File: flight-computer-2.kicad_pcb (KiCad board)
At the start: 4 copper layers, 51 x 51 mm, 0 parts

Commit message: Rough PCB layout
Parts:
- added AE1: 47948-0001, flight-computer-2:47948-0001, F.Cu at (97.5, 58.2)
- added C1: 4.7uF, flight-computer-2:C_0603_1608Metric, F.Cu at (176.9, 78.6)
- added C10: 22pF, flight-computer-2:C_0603_1608Metric, F.Cu at (183.7, 68.1)
- added C11: 22pF, flight-computer-2:C_0603_1608Metric, F.Cu at (187.1, 65.5)
- added C12: 0.1uF, flight-computer-2:C_0603_1608Metric, F.Cu at (165.1, 87.9)
- added C13: 10uF, flight-computer-2:C_0603_1608Metric, F.Cu at (188.6, 62.3)
- added C14: 1uF, flight-computer-2:C_0603_1608Metric, F.Cu at (192.6, 62.3)
- added C15: 0.1uF, flight-computer-2:C_0603_1608Metric, F.Cu at (163.8, 91.4)
- added C16: 0.1uF, flight-computer-2:C_0603_1608Metric, F.Cu at (183.7, 70.6)
- added C17: 10uF, flight-computer-2:C_0603_1608Metric, F.Cu at (174.1, 82.6)
- added C18: 0.1uF, flight-computer-2:C_0603_1608Metric, F.Cu at (186.1, 83.2)
- added C19: 0.1uF, flight-computer-2:C_0603_1608Metric, F.Cu at (179.9, 90.1)
- added C2: 220uF, flight-computer-2:C_1206_3216Metric, F.Cu at (82.5, 56.0)
- added C20: DNP, flight-computer-2:C_0402_1005Metric, F.Cu at (169.5, 85.5)
- added C21: 0.1uF, flight-computer-2:C_0603_1608Metric, F.Cu at (192.9, 74.8)
- added C22: 0.1uF, flight-computer-2:C_0603_1608Metric, F.Cu at (175.9, 92.6)
- added C23: DNP, flight-computer-2:C_0402_1005Metric, F.Cu at (163.3, 93.7)
- added C3: 220uF, flight-computer-2:C_1206_3216Metric, F.Cu at (166.6, 77.1)
- added C4: 220uF, flight-computer-2:C_1206_3216Metric, F.Cu at (113.0, 99.0)
- added C5: 220uF, flight-computer-2:C_1206_3216Metric, F.Cu at (160.4, 84.2)
- added C6: 4.7uF, flight-computer-2:C_0603_1608Metric, F.Cu at (181.1, 86.1)
- added C7: 0.1uF, flight-computer-2:C_0603_1608Metric, F.Cu at (186.1, 80.7)
- added C8: 0.1uF, flight-computer-2:C_0603_1608Metric, F.Cu at (176.9, 76.1)
- added C9: 0.1uF, flight-computer-2:C_0603_1608Metric, F.Cu at (171.4, 80.1)
- added D1: SM5817PL-TP, flight-computer-2:D_SOD-123F, F.Cu at (160.3, 88.5)
- added D2: LTST-C191KGKT, flight-computer-2:LED_0603_1608Metric, F.Cu at (150.8, 93.7)
- added D3: SM5817PL-TP, flight-computer-2:D_SOD-123F, F.Cu at (172.1, 77.1)
- added D4: USBLC6-2SC6, Package_TO_SOT_SMD:SOT-23-6, F.Cu at (99.0, 89.5)
- added D5: LTST-C191KRKT, flight-computer-2:LED_0603_1608Metric, F.Cu at (183.0, 65.6)
- added D6: LTST-C191TBKT, flight-computer-2:LED_0603_1608Metric, F.Cu at (154.9, 93.7)
- added D7: CLMVC-FKA-CL1D1L71BB7C3C3, flight-computer-2:LED_Cree-PLCC4_2x2mm_CW, F.Cu at (178.8, 72.9)
- added H1: MountingHole, MountingHole:MountingHole_2.2mm_M2, F.Cu at (80.0, 60.0)
- added H2: MountingHole, MountingHole:MountingHole_2.2mm_M2, F.Cu at (115.0, 60.0)
- added H3: MountingHole, MountingHole:MountingHole_2.2mm_M2, F.Cu at (115.0, 95.0)
- added H4: MountingHole, MountingHole:MountingHole_2.2mm_M2, F.Cu at (80.0, 95.0)
- added J1: USB4105-GF-A, flight-computer-2:GCT_USB4105-GF-A, F.Cu at (97.5, 97.8)
- added J2: THR, flight-computer-2:PinHeader_1x03_P2.54mm_Vertical, F.Cu at (88.5, 96.0)
- added J3: SER1, flight-computer-2:PinHeader_1x03_P2.54mm_Vertical, F.Cu at (76.0, 56.0)
- added J4: SER2, flight-computer-2:PinHeader_1x03_P2.54mm_Vertical, F.Cu at (119.0, 56.0)
- added J5: SER3, flight-computer-2:PinHeader_1x03_P2.54mm_Vertical, F.Cu at (119.0, 99.0)
- added J6: SER4, flight-computer-2:PinHeader_1x03_P2.54mm_Vertical, F.Cu at (76.0, 99.0)
- added J7: Breakout L, flight-computer-2:PinHeader_1x07_P2.54mm_Vertical, F.Cu at (77.0, 77.5)
- added J8: Breakout R, flight-computer-2:PinHeader_1x07_P2.54mm_Vertical, F.Cu at (118.0, 77.5)
- added L1: 0K, flight-computer-2:L_0402_1005Metric, F.Cu at (194.5, 64.5)
- added R1: 47Ω, flight-computer-2:R_1206_3216Metric, F.Cu at (84.5, 61.0)
- added R10: 10k, flight-computer-2:R_0603_1608Metric, F.Cu at (170.1, 83.3)
- added R11: 10k, flight-computer-2:R_0603_1608Metric, F.Cu at (187.7, 70.6)
- added R12: 10k, flight-computer-2:R_0603_1608Metric, F.Cu at (167.8, 90.4)
- added R13: 10k, flight-computer-2:R_0603_1608Metric, F.Cu at (174.1, 85.1)
- added R14: 10k, flight-computer-2:R_0603_1608Metric, F.Cu at (180.9, 78.6)
- added R15: 1k, flight-computer-2:R_0603_1608Metric, F.Cu at (173.1, 87.6)
- added R16: 1k, flight-computer-2:R_0603_1608Metric, F.Cu at (167.8, 93.0)
- added R17: 2k, flight-computer-2:R_0603_1608Metric, F.Cu at (187.7, 73.1)
- added R18: 10k, flight-computer-2:R_0603_1608Metric, F.Cu at (178.1, 81.1)
- added R19: 4.7k, flight-computer-2:R_0603_1608Metric, F.Cu at (191.7, 67.3)
- added R2: 47Ω, flight-computer-2:R_1206_3216Metric, F.Cu at (183.8, 62.6)
- added R20: 4.7k, flight-computer-2:R_0603_1608Metric, F.Cu at (184.9, 75.7)
- added R21: 22.1k, flight-computer-2:R_0603_1608Metric, F.Cu at (191.7, 69.8)
- added R22: 47.5k, flight-computer-2:R_0603_1608Metric, F.Cu at (178.1, 83.6)
- added R23: 2.2k, flight-computer-2:R_0603_1608Metric, F.Cu at (171.9, 90.4)
- added R24: 2.2k, flight-computer-2:R_0603_1608Metric, F.Cu at (184.9, 78.2)
- added R25: 2k, flight-computer-2:R_0603_1608Metric, F.Cu at (182.1, 81.1)
- added R26: 2k, flight-computer-2:R_0603_1608Metric, F.Cu at (177.1, 87.6)
- added R27: 2k, flight-computer-2:R_0603_1608Metric, F.Cu at (191.7, 72.3)
- added R28: 1k, flight-computer-2:R_0603_1608Metric, F.Cu at (188.9, 75.6)
- added R29: 1k, flight-computer-2:R_0603_1608Metric, F.Cu at (171.9, 93.0)
- added R3: 47Ω, flight-computer-2:R_1206_3216Metric, F.Cu at (111.0, 94.0)
- added R30: 10k, flight-computer-2:R_0603_1608Metric, F.Cu at (182.1, 83.6)
- added R31: 33k, flight-computer-2:R_0603_1608Metric, F.Cu at (175.9, 90.1)
- added R32: 33k, flight-computer-2:R_0603_1608Metric, F.Cu at (188.9, 78.1)
- added R4: 47Ω, flight-computer-2:R_1206_3216Metric, F.Cu at (173.7, 73.2)
- added R5: 5.1k, flight-computer-2:R_0603_1608Metric, F.Cu at (169.1, 87.9)
- added R6: 5.1k, flight-computer-2:R_0603_1608Metric, F.Cu at (183.0, 73.2)
- added R7: 1M, flight-computer-2:R_0603_1608Metric, F.Cu at (180.9, 76.1)
- added R8: 10k, flight-computer-2:R_0603_1608Metric, F.Cu at (187.7, 68.1)
- added R9: 2k, flight-computer-2:R_0603_1608Metric, F.Cu at (191.1, 64.8)
- added SW1: RESET, flight-computer-2:SW_PTS810_SJM_250_SMTR_LFS, F.Cu at (106.5, 97.5)
- added SW2: BOOT, flight-computer-2:SW_PTS810_SJM_250_SMTR_LFS, F.Cu at (106.5, 92.0)
- added U1: AP2114H-3.3TRG1, flight-computer-2:SOT-223, F.Cu at (86.0, 86.0)
- added U2: MUN5214DW1T1G, flight-computer-2:SOT-363_SC-70-6, F.Cu at (105.0, 87.0)
- added U3: BNO080, flight-computer-2:LGA-28_5.2x3.8mm_P0.5mm, F.Cu at (87.0, 74.5)
- added U4: CP2102N, flight-computer-2:QFN-28-1EP_5x5mm_P0.5mm_EP3.35x3.35mm, F.Cu at (100.0, 80.0)
- added U5: MPL3115A2, flight-computer-2:LGA-8_3x5mm_P1.25mm, F.Cu at (109.5, 69.5)
- added U6: ESP32-PICO-D4, flight-computer-2:PQFN50P700X700X104-49N, F.Cu at (97.5, 68.5)
- added Y1: 32.768kHz, flight-computer-2:ABS07, F.Cu at (179.1, 69.3)

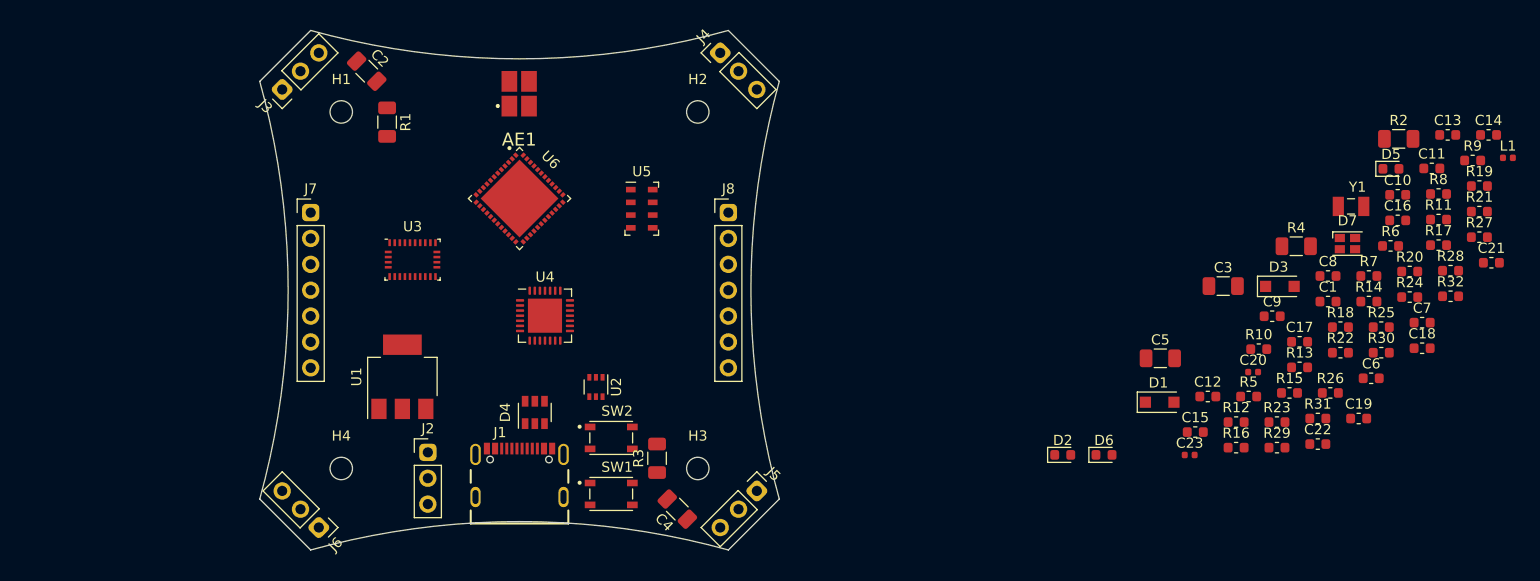
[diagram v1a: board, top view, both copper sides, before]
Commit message: Mounting holes and more component placement
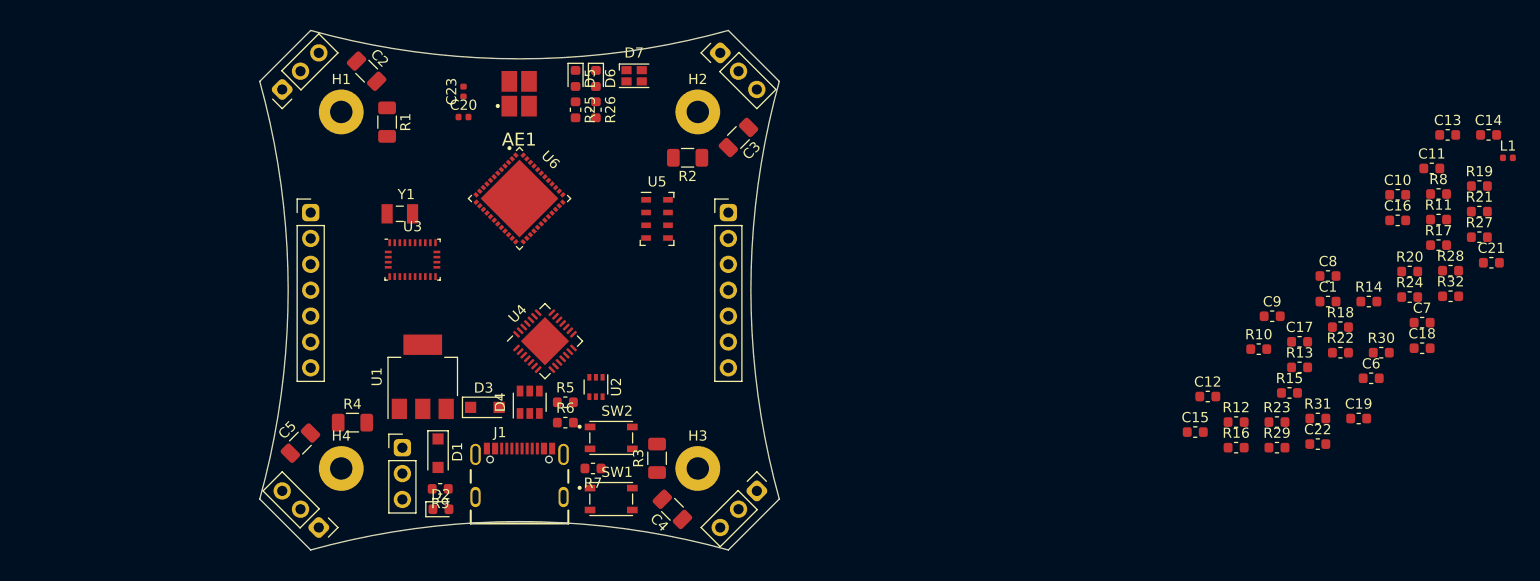
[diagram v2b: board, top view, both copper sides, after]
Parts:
- H1, H2, H3, H4: footprint MountingHole:MountingHole_2.2mm_M2 -> MountingHole:MountingHole_2.2mm_M2_Pad
- moved R9 106.4 mm to (89.7, 97.0), turned to 180 degrees
- moved R4 94.2 mm to (81.1, 90.5)
- moved Y1 93.4 mm to (85.8, 70.0)
- moved C5 84.8 mm to (76.0, 92.5), turned to 45 degrees
- moved R6 82.8 mm to (102.0, 90.5)
- moved R25 81.9 mm to (103.0, 59.8), turned to 270 degrees
- moved C20 81.5 mm to (92.0, 60.5)
- moved D5 80.5 mm to (103.0, 56.7), turned to 270 degrees
- moved C23 79.7 mm to (92.0, 58.0), turned to 90 degrees
- moved D3 78.9 mm to (94.1, 89.0)
- moved R7 78.5 mm to (104.7, 95.0), turned to 180 degrees
- moved R26 77.3 mm to (105.0, 59.8), turned to 270 degrees
- moved D7 71.9 mm to (108.8, 56.5)
- moved D1 71.0 mm to (89.5, 93.5), turned to 270 degrees
- moved R2 69.8 mm to (114.0, 64.5), turned to 180 degrees
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
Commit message: Adjusting 3D model offset and more placement
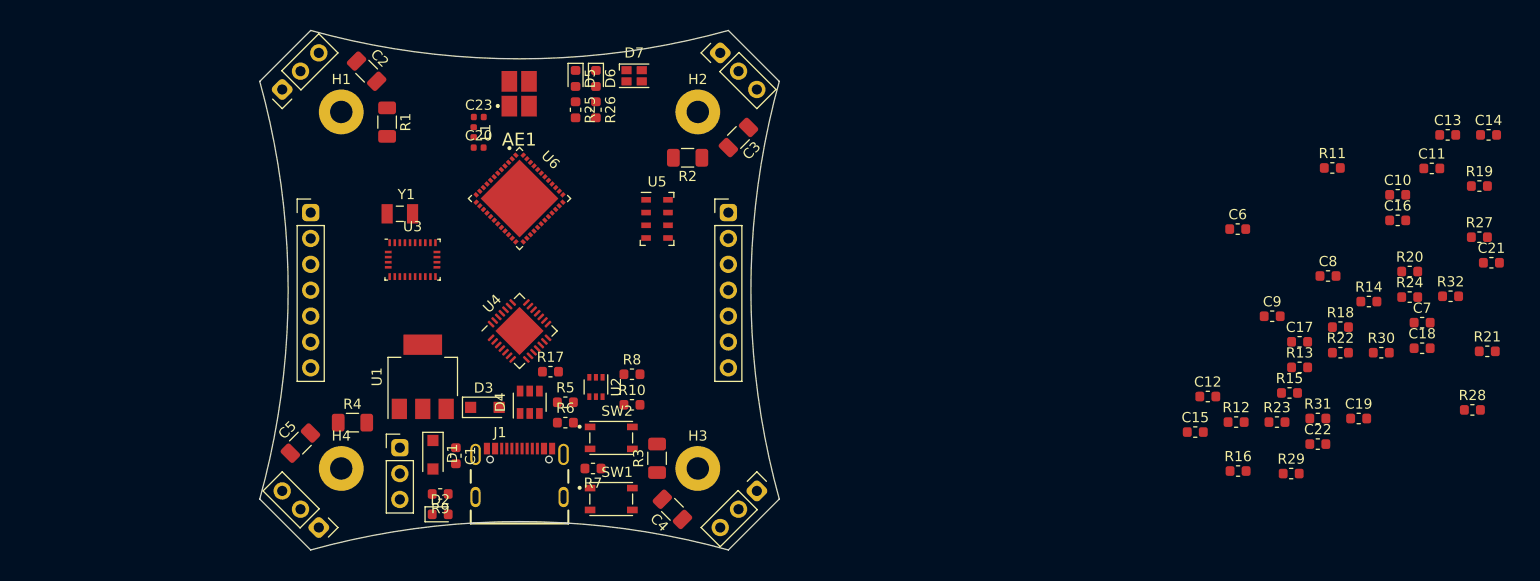
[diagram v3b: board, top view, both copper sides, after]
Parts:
- moved L1 101.6 mm to (93.0, 62.0), turned to 270 degrees
- moved R17 88.1 mm to (100.5, 85.5)
- moved C1 86.9 mm to (91.2, 93.8), turned to 270 degrees
- moved R8 81.1 mm to (108.5, 85.8)
- moved R10 61.8 mm to (108.5, 88.8)
- moved C6 19.7 mm to (168.0, 71.5)
- moved R28 13.8 mm to (191.0, 89.2)
- moved R21 13.7 mm to (192.5, 83.5)
- moved R11 11.6 mm to (177.3, 65.5)
- moved C20 3.35 mm to (93.5, 63.5)
- moved C23 2.92 mm to (93.5, 60.5), turned to 0 degrees
- moved R29 2.90 mm to (173.2, 95.5)
- moved U4 2.69 mm to (97.5, 81.5)
- moved R16 2.30 mm to (168.0, 95.2)
- moved D1 0.52 mm to (89.0, 93.7)
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
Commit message: More placement and footprint updates
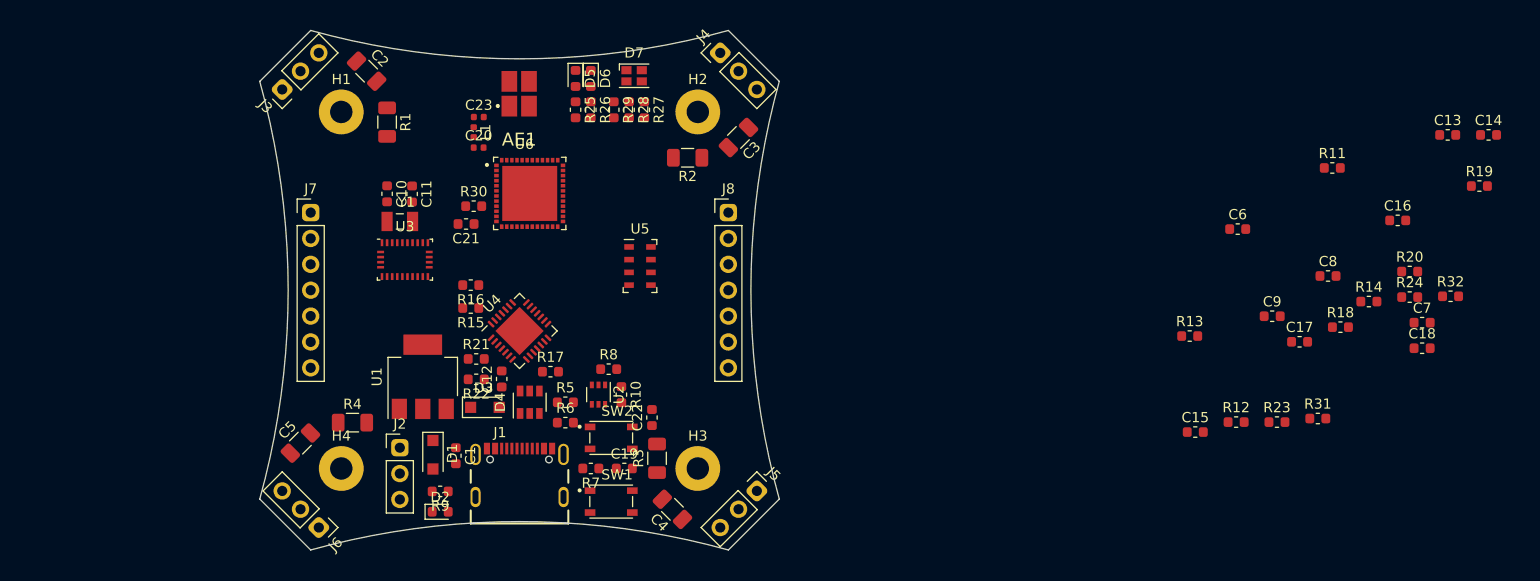
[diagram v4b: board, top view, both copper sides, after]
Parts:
- moved C21 100.7 mm to (92.2, 71.0), turned to 180 degrees
- moved C11 100.1 mm to (87.0, 68.1), turned to 270 degrees
- moved R21 99.3 mm to (93.2, 84.2)
- moved C10 99.2 mm to (84.5, 68.0), turned to 270 degrees
- moved R30 90.2 mm to (93.0, 69.2)
- moved R28 87.9 mm to (108.2, 59.8), turned to 270 degrees
- moved R22 84.9 mm to (93.2, 86.2), turned to 180 degrees
- moved R27 82.9 mm to (109.8, 59.8), turned to 270 degrees
- moved R15 80.8 mm to (92.7, 79.2), turned to 180 degrees
- moved R16 77.5 mm to (92.7, 77.0), turned to 180 degrees
- moved R29 75.5 mm to (106.8, 59.8), turned to 270 degrees
- moved C19 72.3 mm to (107.8, 95.0)
- moved C12 69.3 mm to (95.8, 86.2), turned to 90 degrees
- moved C22 65.4 mm to (110.5, 90.0), turned to 90 degrees
- moved R13 11.2 mm to (163.3, 82.0)
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
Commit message: Finished preliminary placement
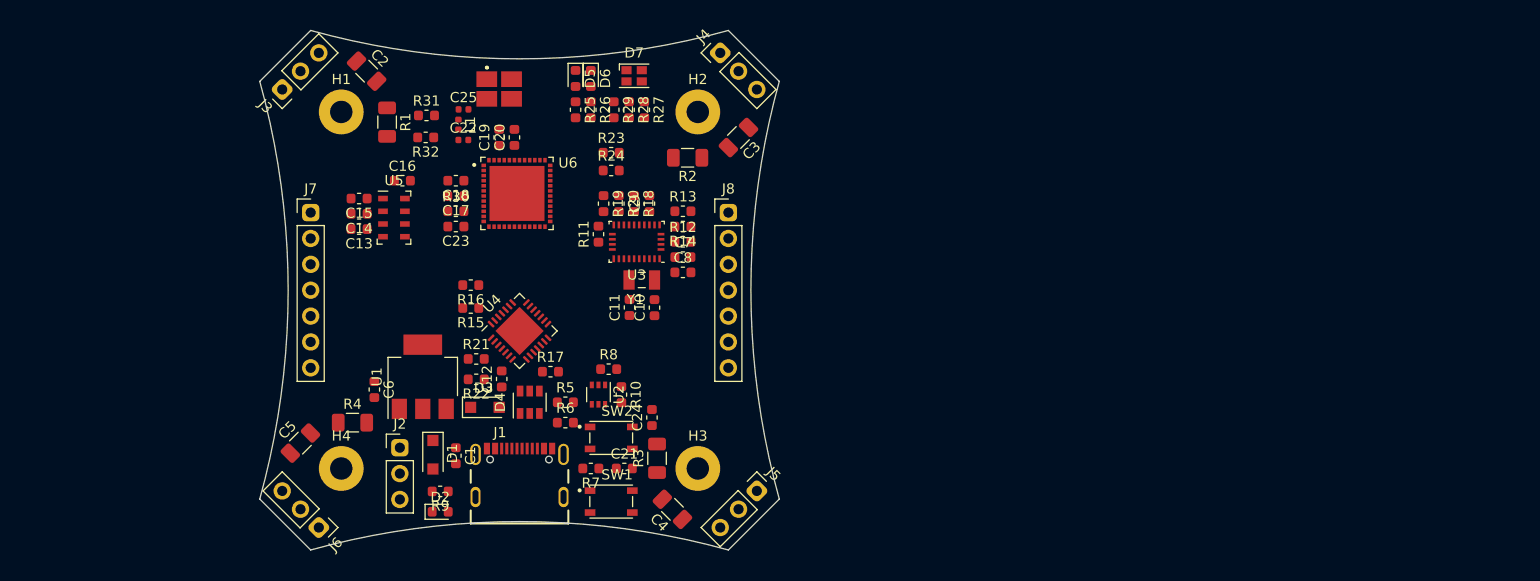
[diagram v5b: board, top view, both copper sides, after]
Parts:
- added C19: 10uF, flight-computer-2:C_0603_1608Metric, F.Cu at (95.5, 62.5)
- added C20: 0.1uF, flight-computer-2:C_0603_1608Metric, F.Cu at (97.0, 62.5)
- moved C14 111.1 mm to (81.8, 70.0), turned to 180 degrees
- moved C13 107.3 mm to (81.8, 71.5), turned to 180 degrees
- moved R32 101.8 mm to (88.3, 62.5), turned to 180 degrees
- moved C16 97.8 mm to (86.0, 66.8)
- moved C18 96.3 mm to (91.2, 66.8), turned to 180 degrees
- moved R31 92.4 mm to (88.4, 60.3)
- moved C6 86.2 mm to (83.2, 87.2), turned to 270 degrees
- moved R19 86.0 mm to (105.8, 69.0), turned to 270 degrees
- moved C15 85.2 mm to (81.8, 68.5), turned to 180 degrees
- moved C17 84.1 mm to (91.2, 68.2), turned to 180 degrees
- moved R24 79.4 mm to (106.5, 65.8)
- moved R20 77.9 mm to (107.2, 69.0), turned to 270 degrees
- moved C7 72.9 mm to (113.5, 74.2)
- moved R11 72.3 mm to (105.2, 72.0), turned to 90 degrees
- moved R23 70.5 mm to (106.5, 64.0)
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- renumbered C19 to C21, C20 to C22, C21 to C23, C22 to C24, C23 to C25

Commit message: More layout and routing
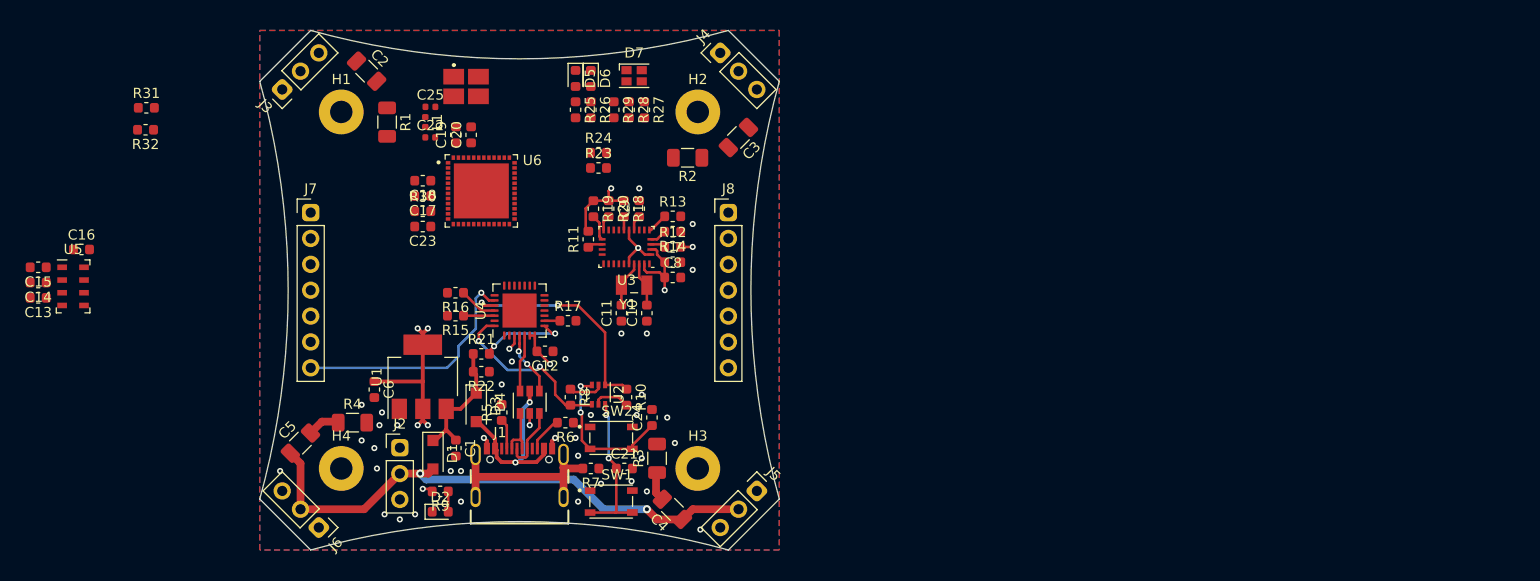
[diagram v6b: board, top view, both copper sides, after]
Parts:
- moved C13 32.2 mm to (50.2, 78.2)
- moved C14 32.2 mm to (50.2, 76.8)
- moved C15 32.2 mm to (50.2, 75.2)
- moved C16 32.2 mm to (54.5, 73.5)
- moved U5 32.2 mm to (53.7, 77.1)
- moved R31 27.5 mm to (60.9, 59.6)
- moved R32 27.5 mm to (60.8, 61.8)
- moved R5 6.33 mm to (95.8, 89.5), turned to 90 degrees
- moved R17 5.29 mm to (102.2, 80.5)
- moved C12 5.04 mm to (100.0, 83.5), turned to 180 degrees
- moved R8 4.65 mm to (102.5, 88.0), turned to 270 degrees
- moved C19 4.26 mm to (91.2, 62.2)
- moved C20 4.26 mm to (92.8, 62.2)
- moved U6 3.51 mm to (93.8, 67.8)
- moved AE1 3.26 mm to (92.2, 57.5)
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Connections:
- D4 pad 4: /D- -> /D+
- D4 pad 6: /D+ -> /D-
- J1 pad A6: Net-(D4-Pad1) -> Net-(D4-Pad3)
- J1 pad A7: Net-(D4-Pad3) -> Net-(D4-Pad1)
- J1 pad B6: Net-(D4-Pad1) -> Net-(D4-Pad3)
- J1 pad B7: Net-(D4-Pad3) -> Net-(D4-Pad1)
- J7 pad 1: /VIN -> GND
- J7 pad 2: +3V3 -> /VBEC
- J7 pad 3: /IO4 -> +3V3
- J7 pad 4: /IO5 -> /IO13
- J7 pad 5: /SCL -> /RTS
- J7 pad 6: /SDA -> /IO15
- J7 pad 7: GND -> /CTS
- J8 pad 1: /RTS -> GND
- J8 pad 2: /IO13 -> /IO4
- J8 pad 3: /CTS -> /IO5
- J8 pad 4: /IO15 -> /SCL
- J8 pad 5: /IO9 -> /SDA
- J8 pad 6: /IO10 -> /IO9
- J8 pad 7: GND -> /IO10
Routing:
- net /VBEC: track 0.00 -> 54.1 mm, vias 0 -> 2
- net +3V3: track 0.00 -> 37.7 mm, vias 0 -> 9
- net /CTS: track 0.00 -> 23.8 mm, vias 0 -> 1
- net /RTS: track 0.00 -> 22.1 mm, vias 0 -> 2
- net Net-(J1-PadG1): track 0.00 -> 19.0 mm
- net Net-(D3-Pad2): track 0.00 -> 17.9 mm, vias 0 -> 2
- net /DTR: track 0.00 -> 17.4 mm, vias 0 -> 2
- net /EN: track 0.00 -> 15.3 mm, vias 0 -> 2
- net /IO0: track 0.00 -> 14.9 mm, vias 0 -> 2
- net /VIN: track 0.00 -> 12.8 mm
- net GND: track 0.00 -> 10.6 mm, vias 0 -> 40
- net Net-(R21-Pad2): track 0.00 -> 8.82 mm, vias 0 -> 2
- net Net-(D4-Pad3): track 0.00 -> 6.50 mm
- net /D+: track 0.00 -> 6.32 mm, vias 0 -> 2
- net /D-: track 0.00 -> 5.64 mm
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- added copper zone on In2.Cu, net +3V3
- added copper zone on B.Cu, net GND
- added copper zone on F.Cu, net GND
- added copper zone on In1.Cu, net GND
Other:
- net class Default: clearance 0.2 -> 0.1524; trace_width 0.25 -> 0.1524; via_dia 0.8 -> 0.6; via_drill 0.4 -> 0.3
- rule trace_clearance: 0.2 -> 0.1524
- rule trace_min: 0.2 -> 0.1524
- rule via_min_size: 0.4 -> 0.6
